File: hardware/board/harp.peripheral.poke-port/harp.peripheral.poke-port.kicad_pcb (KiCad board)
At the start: 4 copper layers, 26.3 x 26.3 mm, 21 parts, among them J1 Conn_01x03_Socket, U1 TPS63060, U2 EE-SX1140, U3 74LVCH2T45DC

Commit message: add 3d models
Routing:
- added copper zone on F.Cu, net GND
- removed copper zone on In1.Cu, net GND
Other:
- copper layers 4 -> 2
- board text added: "0356-E- 002-001. 000.000"
- board text added: "GND"
- board text added: "M2"
- board text added: "Sonya Vasquez Feb 3, 2025"
- board text added: "TTL ↑ POKE"
- board text added: "Vpp"
- board text added: "harp.peripheral.poke-port"
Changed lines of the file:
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@@
 	(layers
 		(0 "F.Cu" signal)
-		(1 "In1.Cu" power)
-		(2 "In2.Cu" power)
 		(31 "B.Cu" signal)
 		(32 "B.Adhes" user "B.Adhesive")
@@
 			)
 			(layer "dielectric 1"
-				(type "prepreg")
-				(thickness 0.2021)
-				(material "FR4")
-				(epsilon_r 4.5)
-				(loss_tangent 0.02)
-			)
-			(layer "In1.Cu"
-				(type "copper")
-				(thickness 0.0175)
-			)
-			(layer "dielectric 2"
 				(type "core")
-				(thickness 0.9906)
-				(material "FR4")
-				(epsilon_r 4.5)
-				(loss_tangent 0.02)
-			)
-			(layer "In2.Cu"
-				(type "copper")
-				(thickness 0.0175)
-			)
-			(layer "dielectric 3"
-				(type "prepreg")
-				(thickness 0.2021)
+				(thickness 1.4298)
 				(material "FR4")
 				(epsilon_r 4.5)
@@
 		(at 155.8 98.85)
 		(property "Reference" "J1"
-			(at -0.1 9.15 0)
+			(at 0 7.35 0)
 			(unlocked yes)
 			(layer "F.SilkS")
@@
 			(pintype "passive")
 		)
+		(model "/home/poofjunior/projects/kicad_libraries/kicad-lib/kicad-lib.3dshapes/3M_Mini-Clamp_37203-62B3-003 PL.stp"
+			(offset
+				(xyz -5.8 -21.85 -5.42)
+			)
+			(scale
+				(xyz 1 1 1)
+			)
+			(rotate
+				(xyz 0 0 -90)
+			)
+		)
 	)
 	(footprint "kicad-lib:EE-SX1140"
@@
 		(at 150 100 -90)
 		(property "Reference" "U2"
-			(at 0 3.53 90)
+			(at -2.7 0 180)
 			(unlocked yes)
 			(layer "B.SilkS")
 			(effects
 				(font
-					(size 1 1)
-					(thickness 0.15)
+					(size 0.8 0.8)
+					(thickness 0.125)
 				)
 				(justify mirror)
@@
 			(pintype "passive")
 		)
+		(model "/home/poofjunior/projects/kicad_libraries/kicad-lib/kicad-lib.3dshapes/Omron_EE_SX1140.step"
+			(offset
+				(xyz -9.95 -0.97 0)
+			)
+			(scale
+				(xyz 1 1 1)
+			)
+			(rotate
+				(xyz -90 0 0)
+			)
+		)
 	)
 	(gr_circle
@@
 		(layer "Edge.Cuts")
 	)
+	(gr_text "Sonya Vasquez\nFeb 3, 2025"
+		(at 141.3 93.88 90)
+		(layer "B.SilkS")
+		(effects
+			(font
+				(size 1 1)
+				(thickness 0.2)
+			)
+			(justify left bottom mirror)
+		)
+	)
+	(gr_text "harp.peripheral.poke-port"
+		(at 146.4 87.9 90)
+		(layer "B.SilkS")
+		(effects
+			(font
+				(size 1 1)
+				(thickness 0.2)
+			)
+			(justify left bottom mirror)
+		)
+	)
+	(gr_text "GND"
+		(at 159 97.8 0)
+		(layer "F.SilkS")
+		(effects
+			(font
+				(size 1 1)
+				(thickness 0.2)
+				(bold yes)
+			)
+			(justify left bottom)
+		)
+	)
+	(gr_text "TTL ↑\nPOKE"
+		(at 162.2 104.4 90)
+		(layer "F.SilkS")
+		(effects
+			(font
+				(size 1 1)
+				(thickness 0.2)
+			)
+			(justify left bottom)
+		)
+	)
+	(gr_text "M2"
+		(at 146.2 112.3 0)
+		(layer "F.SilkS")
+		(effects
+			(font
+				(size 1 1)
+				(thickness 0.2)
+			)
+			(justify left bottom)
+		)
+	)
+	(gr_text "0356-E-\n002-001.\n000.000"
+		(at 151.9 111 0)
+		(layer "F.SilkS")
+		(effects
+			(font
+				(size 0.8 0.8)
+				(thickness 0.125)
+			)
+			(justify left bottom)
+		)
+	)
+	(gr_text "Vpp"
+		(at 159.2 99.4 0)
+		(layer "F.SilkS")
+		(effects
+			(font
+				(size 1 1)
+				(thickness 0.2)
+				(bold yes)
+			)
+			(justify left bottom)
+		)
+	)
+	(gr_text "M2"
+		(at 151.5 88.9 0)
+		(layer "F.SilkS")
+		(effects
+			(font
+				(size 1 1)
+				(thickness 0.2)
+			)
+			(justify left bottom)
+		)
+	)
 	(segment
 		(start 141.825 104.65)
@@
 		(layer "F.Cu")
 		(hatch edge 0.5)
+		(priority 2)
 		(connect_pads yes
 			(clearance 0.25)
@@
 		(layer "F.Cu")
 		(hatch edge 0.5)
+		(priority 2)
 		(connect_pads yes
 			(clearance 0.25)
@@
 		(net 1)
 		(net_name "GND")
-		(layers "In1.Cu" "B.Cu")
+		(layers "F&B.Cu")
 		(hatch edge 0.5)
 		(priority 1)

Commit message: update silkscreen
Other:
- board text added: "5V TTL ↑ POKE"
- board text added: "Vin"
- board text added: "Vin: 2.5-12V"
- board text removed: "TTL ↑ POKE"
- board text removed: "Vpp"
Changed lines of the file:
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@@
 		(tags "resistor")
 		(property "Reference" "R3"
-			(at 2.3 0 0)
+			(at -2.2 0 0)
 			(layer "F.SilkS")
 			(effects
@@
 		)
 	)
+	(gr_text "Vin:\n2.5-12V"
+		(at 147.9 91.6 0)
+		(layer "F.SilkS")
+		(effects
+			(font
+				(size 1 1)
+				(thickness 0.2)
+				(bold yes)
+			)
+			(justify right bottom)
+		)
+	)
 	(gr_text "GND"
 		(at 159 97.8 0)
@@
 		)
 	)
-	(gr_text "TTL ↑\nPOKE"
-		(at 162.2 104.4 90)
+	(gr_text "5V TTL ↑\nPOKE"
+		(at 162.3 100.1 90)
 		(layer "F.SilkS")
 		(effects
@@
 				(thickness 0.2)
 			)
-			(justify left bottom)
+			(justify right bottom)
 		)
 	)
@@
 		)
 	)
-	(gr_text "Vpp"
+	(gr_text "Vin"
 		(at 159.2 99.4 0)
 		(layer "F.SilkS")

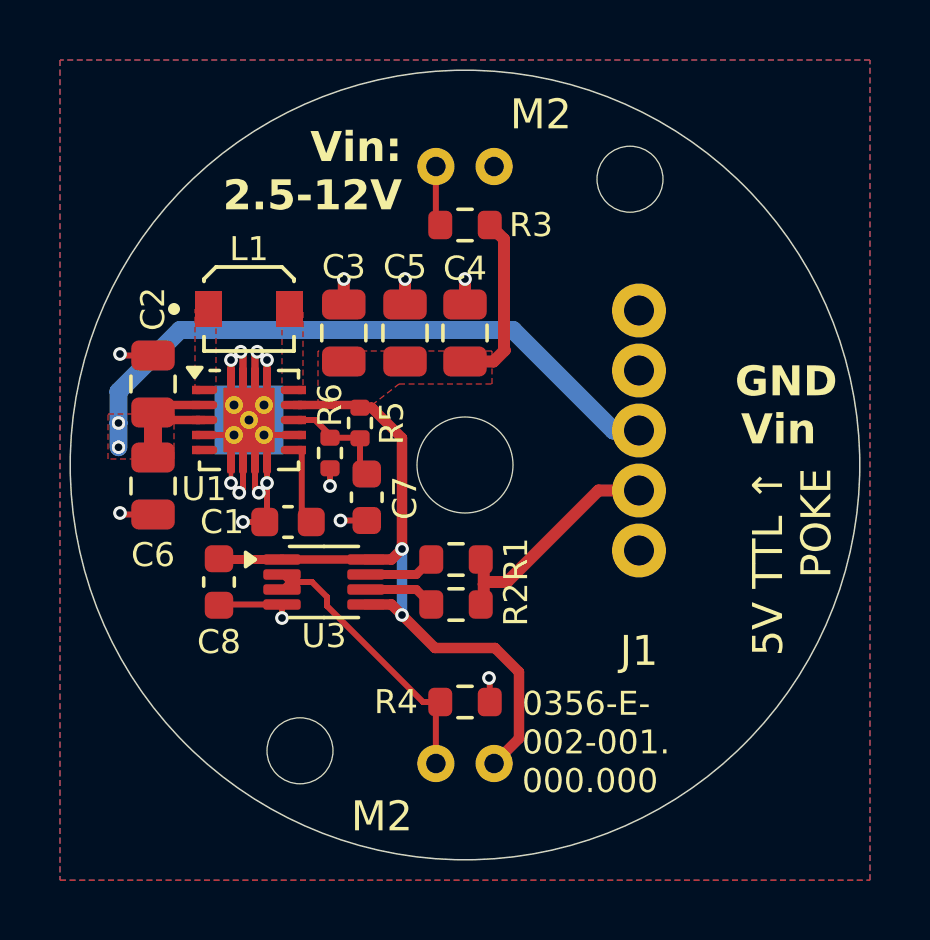
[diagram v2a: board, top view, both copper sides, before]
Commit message: update min soldermask bridge to 0.2mm
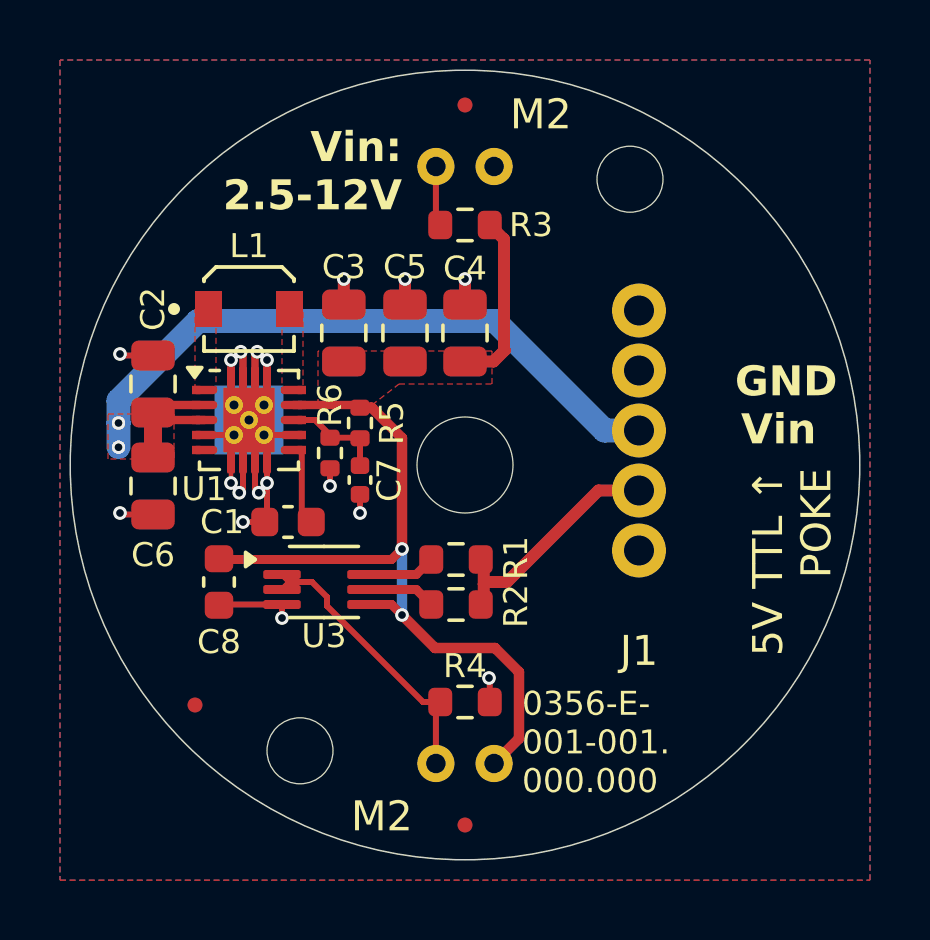
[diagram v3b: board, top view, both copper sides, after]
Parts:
- added REF**: Fiducial_0.5mm_Mask1.5mm, Fiducial:Fiducial_0.5mm_Mask1.5mm, F.Cu at (150.0, 112.0)
- added REF**: Fiducial_0.5mm_Mask1.5mm, Fiducial:Fiducial_0.5mm_Mask1.5mm, F.Cu at (141.0, 108.0)
- added REF**: Fiducial_0.5mm_Mask1.5mm, Fiducial:Fiducial_0.5mm_Mask1.5mm, F.Cu at (150.0, 88.0)
- C7: value 1pF -> 10pF; footprint Capacitor_SMD:C_0603_1608Metric -> Capacitor_SMD:C_0402_1005Metric
- L1: footprint kicad-lib:1226AS-H-1R5N=P2 -> kicad-lib:L_Murata_1226AS-H-1R5N=P2
- R3: value R -> 127
- R4: value R -> 100
- moved C7 0.62 mm to (146.5, 100.5)
- turned R4 to 0 degrees
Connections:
- R4 pad 1: GND -> /POKE
- R4 pad 2: /POKE -> GND
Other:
- board text added: "0356-E- 001-001. 000.000"
- board text removed: "0356-E- 002-001. 000.000"
